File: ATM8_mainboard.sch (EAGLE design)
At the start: 21 parts, among them IC1_POSUV MEGA8-P, IC2_VRETENO MEGA8-P, J1 22-27-2021-02, J2 22-27-2021-02

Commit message: Posledne upravy v dokumente. Nejasne su Dorazy a GVI ci maju byt pripojene na mikrocip alebo priamo len na LPT????
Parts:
- added OUT_POSUV: (no value), con-lstb:MA03-2
- added SV4: (no value), con-lstb:MA05-2
- renumbered SV1 to IO_LPT, SV2 to DISP_1, SV3 to DISP_2
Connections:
- removed net DX: IO_LPT.5
- removed net DZ: IO_LPT.9
- removed net MISO: IC1_POSUV.PB4(MISO), IC2_VRETENO.PB4(MISO), ISP.1, ISP1.1
- removed net MOSI: IC1_POSUV.PB3(MOSI/OC2), IC2_VRETENO.PB3(MOSI/OC2), ISP.4, ISP1.4
- removed net PB0: IC1_POSUV.PB0(ICP), IC2_VRETENO.PB0(ICP)
- removed net PC3: IC1_POSUV.PC3(ADC3), IC2_VRETENO.PC3(ADC3)
- removed net PD0: IC1_POSUV.PD0(RXD)
- removed net PD1: IC1_POSUV.PD1(TXD)
- removed net PD2: IC1_POSUV.PD2(INT0)
- removed net PD3: IC1_POSUV.PD3(INT1), IC2_VRETENO.PD3(INT1)
- removed net PD5: IC1_POSUV.PD5(T1), IC2_VRETENO.PD5(T1)
- removed net PD6: IC1_POSUV.PD6(AIN0), IC2_VRETENO.PD6(AIN0)
- removed net PD7: IC1_POSUV.PD7(AIN1), IC2_VRETENO.PD7(AIN1)
- removed net RESET: IC1_POSUV.PC6(/RESET), IC2_VRETENO.PC6(/RESET), ISP.5, ISP1.5, R1.2, R2.2
- removed net SCK: IC1_POSUV.PB5(SCK), IC2_VRETENO.PB5(SCK), ISP.3, ISP1.3
- removed net SX: IO_LPT.3
- removed net SZ: IO_LPT.7
- new net +Z: IC1_POSUV.PB2(SS/OC1B), OUT_POSUV.5
- new net -Z: IC1_POSUV.PB1(OC1A), OUT_POSUV.3
- new net DIRVRET: IC2_VRETENO.PD6(AIN0)
- new net DIRX: IC1_POSUV.PD0(RXD), IO_LPT.5
- new net DIRZ: IC1_POSUV.PD2(INT0), IO_LPT.9
- new net MISO1: IC1_POSUV.PB4(MISO), ISP.1, OUT_POSUV.6
- new net MISO2: IC2_VRETENO.PB4(MISO), ISP1.1, SV4.9
- new net MOSI1: IC1_POSUV.PB3(MOSI/OC2), ISP.4, OUT_POSUV.4
- new net MOSI2: IC2_VRETENO.PB3(MOSI/OC2), ISP1.4, SV4.7
- new net PB12: IC2_VRETENO.PB1(OC1A)
- new net PB22: IC2_VRETENO.PB2(SS/OC1B)
- new net PC01: IC1_POSUV.PC0(ADC0)
- new net PC02: IC2_VRETENO.PC0(ADC0)
- new net PC11: IC1_POSUV.PC1(ADC1)
- new net PC12: IC2_VRETENO.PC1(ADC1)
- new net PC21: IC1_POSUV.PC2(ADC2)
- new net PC22: IC2_VRETENO.PC2(ADC2)
- new net PC31: IC1_POSUV.PC3(ADC3)
- new net PC32: IC2_VRETENO.PC3(ADC3)
- new net PD32: IC2_VRETENO.PD3(INT1)
- new net PD42: IC2_VRETENO.PD4(XCK/T0)
- new net PD52: IC2_VRETENO.PD5(T1)
- new net PD71: IC1_POSUV.PD7(AIN1)
- new net RESET1: IC1_POSUV.PC6(/RESET), ISP.5, R1.2
- new net RESET2: IC2_VRETENO.PC6(/RESET), ISP1.5, R2.2
- new net SCK1: IC1_POSUV.PB5(SCK), ISP.3
- new net SCK2: IC2_VRETENO.PB5(SCK), ISP1.3, SV4.10
- new net STEPX: IC1_POSUV.PD1(TXD), IO_LPT.3
- new net STEPZ: IC1_POSUV.PD3(INT1), IO_LPT.7
- net DORX: now also IC1_POSUV.PD5(T1)
- net DORZ: now also IC1_POSUV.PD6(AIN0)
- net ENABLE: now also IC1_POSUV.PB0(ICP), IC2_VRETENO.PD7(AIN1)
- net GND: now also OUT_POSUV.1, OUT_POSUV.2, SV4.1, SV4.2
- net PB1: now also SV4.3; no longer IC1_POSUV.PB1(OC1A), IC2_VRETENO.PB1(OC1A)
- net PB2: now also SV4.5; no longer IC1_POSUV.PB2(SS/OC1B), IC2_VRETENO.PB2(SS/OC1B)
- net PC0: now also SV4.8; no longer IC1_POSUV.PC0(ADC0), IC2_VRETENO.PC0(ADC0)
- net PC1: now also SV4.6; no longer IC1_POSUV.PC1(ADC1), IC2_VRETENO.PC1(ADC1)
- net PC2: now also SV4.4; no longer IC1_POSUV.PC2(ADC2), IC2_VRETENO.PC2(ADC2)
- net PD4: no longer IC2_VRETENO.PD4(XCK/T0)
- net PWMV: now also IC2_VRETENO.PB0(ICP)

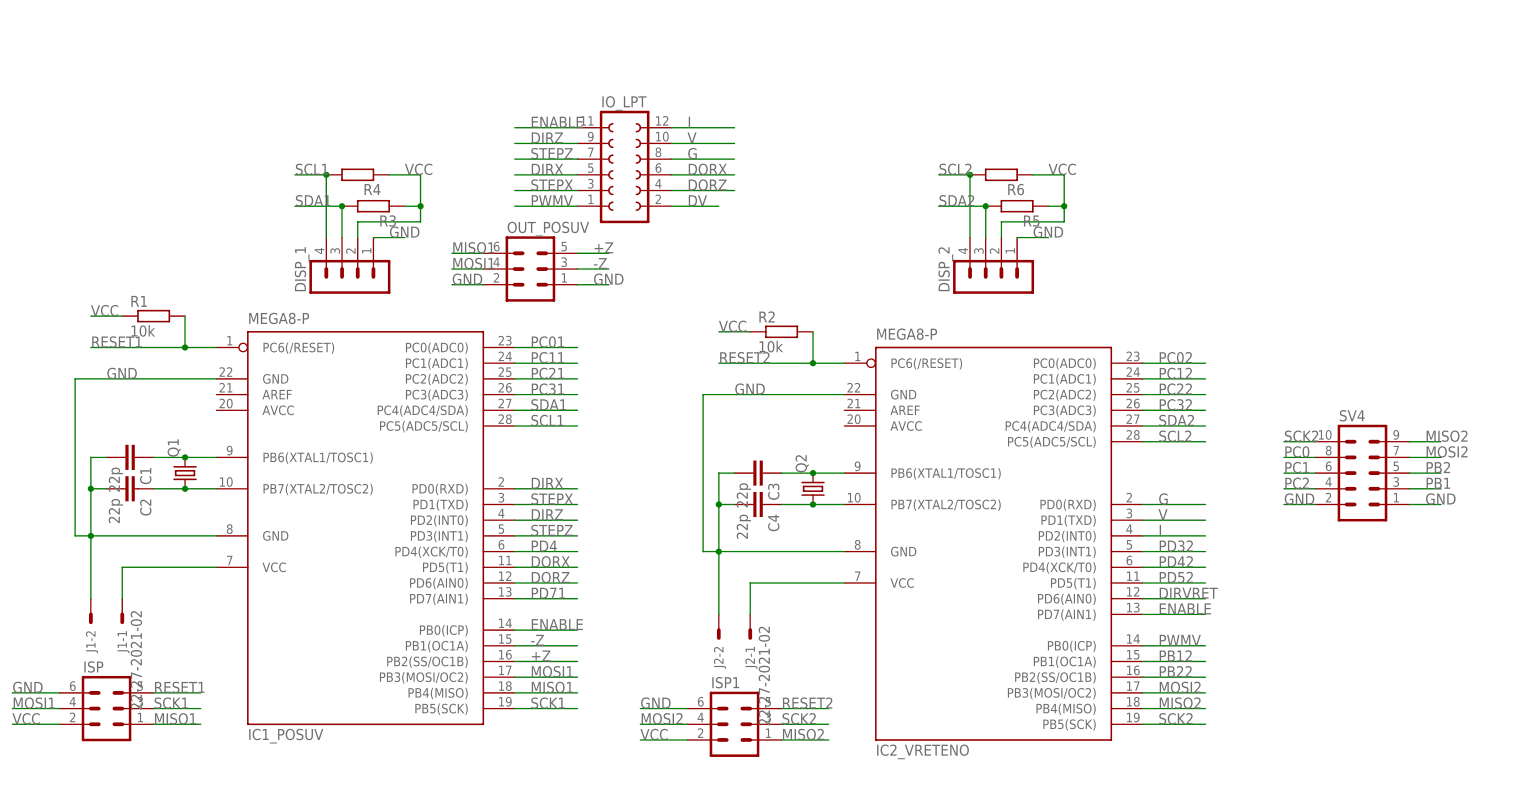
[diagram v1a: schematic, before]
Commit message: Uprava... Pribudlo M01,M02,M03 ale ZMM neviem kam pripojit. Na to sa zabudlo... Predosle problemy pretrvavaju....
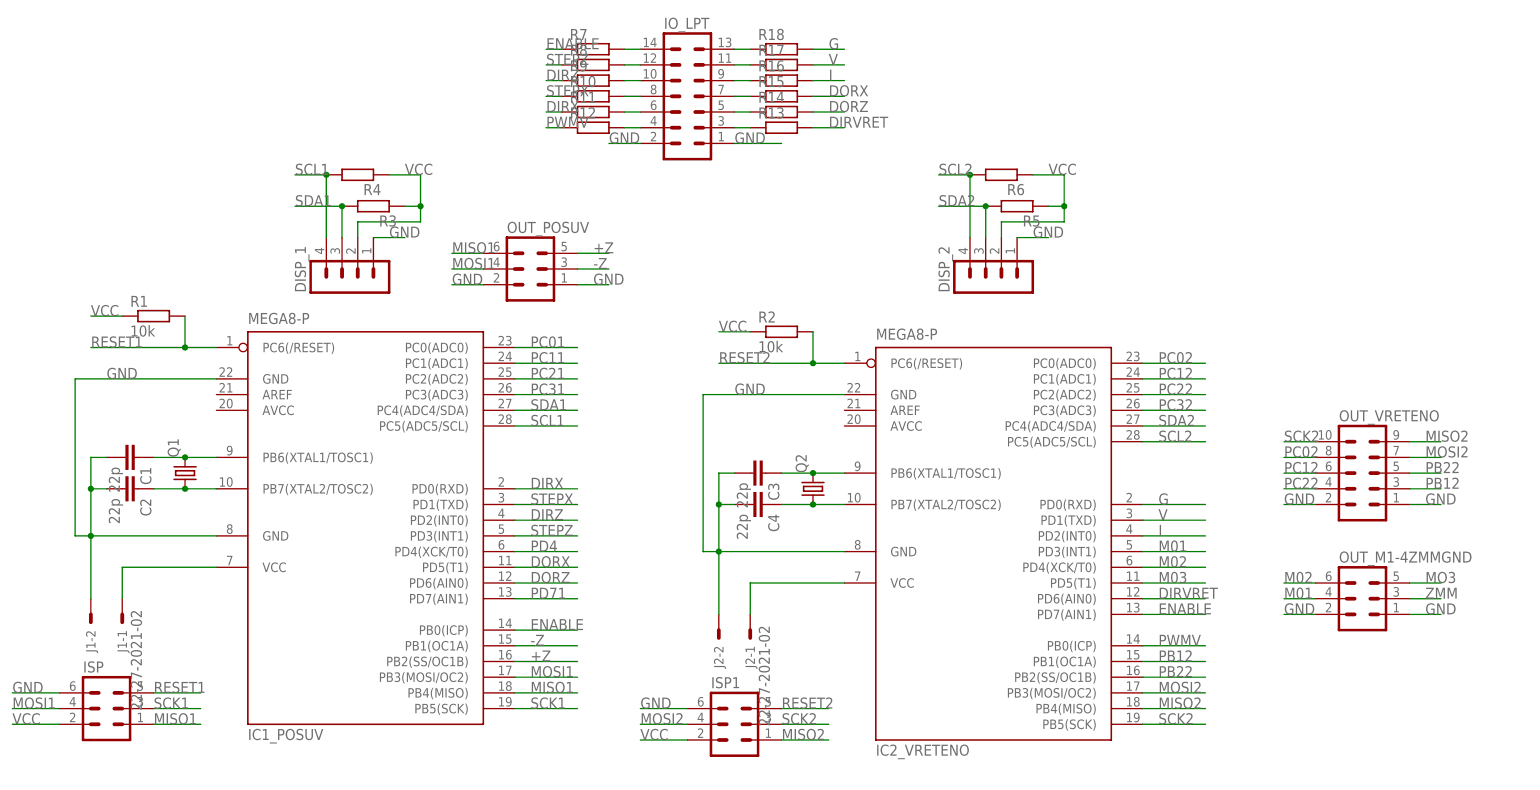
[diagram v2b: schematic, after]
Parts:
- added OUT_M1-4ZMMGND: (no value), con-lstb:MA03-2
- added R10, R11, R12, R13, R14, R15, R16, R17, R18, R7, R8, R9: (no value), resistor:R-EU_0207/10
- IO_LPT: device con-lsta:FE06-2 -> con-lstb:MA07-2
- renumbered SV4 to OUT_VRETENO
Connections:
- net PD52 renamed M03
- removed net DV: IO_LPT.2
- removed net PB1: OUT_VRETENO.3
- removed net PB2: OUT_VRETENO.5
- removed net PC0: OUT_VRETENO.8
- removed net PC1: OUT_VRETENO.6
- removed net PC2: OUT_VRETENO.4
- removed net PD32: IC2_VRETENO.PD3(INT1)
- removed net PD42: IC2_VRETENO.PD4(XCK/T0)
- new net M01: IC2_VRETENO.PD3(INT1), OUT_M1-4ZMMGND.4
- new net M02: IC2_VRETENO.PD4(XCK/T0), OUT_M1-4ZMMGND.6
- new net MO3: OUT_M1-4ZMMGND.5
- new net N$1: IO_LPT.4, R12.2
- new net N$10: IO_LPT.7, R15.1
- new net N$11: IO_LPT.5, R14.1
- new net N$12: IO_LPT.3, R13.1
- new net N$2: IO_LPT.6, R11.2
- new net N$3: IO_LPT.8, R10.2
- new net N$4: IO_LPT.10, R9.2
- new net N$5: IO_LPT.12, R8.2
- new net N$6: IO_LPT.14, R7.2
- new net N$7: IO_LPT.13, R18.1
- new net N$8: IO_LPT.11, R17.1
- new net N$9: IO_LPT.9, R16.1
- new net ZMM: OUT_M1-4ZMMGND.3
- net DIRVRET: now also R13.2
- net DIRX: now also R11.1; no longer IO_LPT.5
- net DIRZ: now also R9.1; no longer IO_LPT.9
- net DORX: now also R15.2; no longer IO_LPT.6
- net DORZ: now also R14.2; no longer IO_LPT.4
- net ENABLE: now also R7.1; no longer IO_LPT.11
- net G: now also R18.2; no longer IO_LPT.8
- net GND: now also IO_LPT.1, IO_LPT.2, OUT_M1-4ZMMGND.1, OUT_M1-4ZMMGND.2
- net I: now also R16.2; no longer IO_LPT.12
- net PB12: now also OUT_VRETENO.3
- net PB22: now also OUT_VRETENO.5
- net PC02: now also OUT_VRETENO.8
- net PC12: now also OUT_VRETENO.6
- net PC22: now also OUT_VRETENO.4
- net PWMV: now also R12.1; no longer IO_LPT.1
- net STEPX: now also R10.1; no longer IO_LPT.3
- net STEPZ: now also R8.1; no longer IO_LPT.7
- net V: now also R17.2; no longer IO_LPT.10

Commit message: 
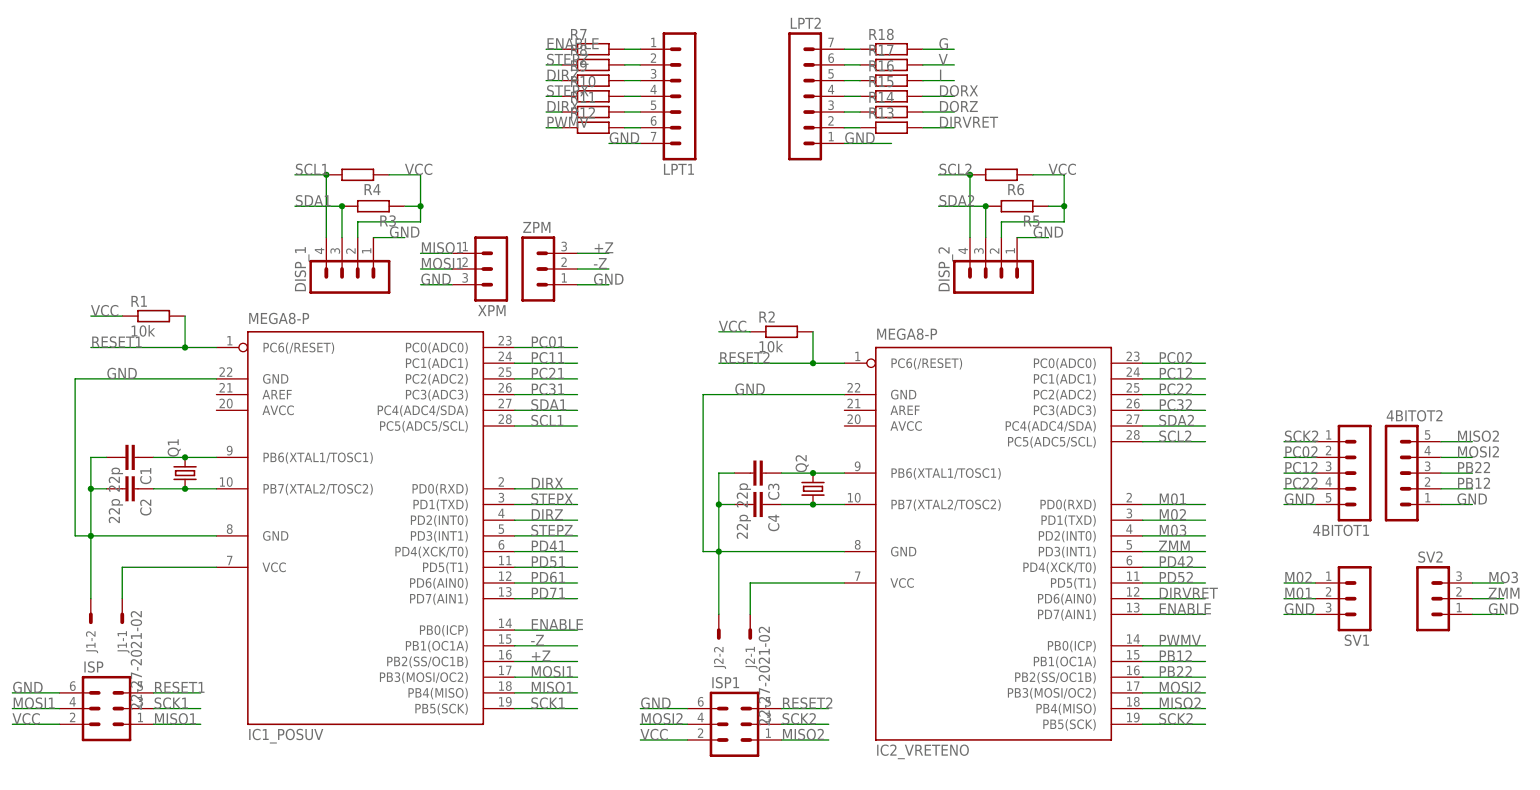
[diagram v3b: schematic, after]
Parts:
- removed IO_LPT: (no value), con-lstb:MA07-2
- removed OUT_M1-4ZMMGND, OUT_POSUV: (no value), con-lstb:MA03-2
- removed OUT_VRETENO: (no value), con-lstb:MA05-2
- added 4BITOT1, 4BITOT2: (no value), con-lstb:MA05-1
- added LPT1, LPT2: (no value), con-lstb:MA07-1
- added SV1, SV2, XPM, ZPM: (no value), con-lstb:MA03-1
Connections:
- net PD4 renamed PD41
- new net PD42: IC2_VRETENO.PD4(XCK/T0)
- new net PD51: IC1_POSUV.PD5(T1)
- new net PD52: IC2_VRETENO.PD5(T1)
- new net PD61: IC1_POSUV.PD6(AIN0)
- net +Z: now also ZPM.3; no longer OUT_POSUV.5
- net -Z: now also ZPM.2; no longer OUT_POSUV.3
- net DORX: no longer IC1_POSUV.PD5(T1)
- net DORZ: no longer IC1_POSUV.PD6(AIN0)
- net G: no longer IC2_VRETENO.PD0(RXD)
- net GND: now also 4BITOT1.5, 4BITOT2.1, LPT1.7, LPT2.1, SV1.3, SV2.1, XPM.3, ZPM.1; no longer IO_LPT.1, IO_LPT.2, OUT_M1-4ZMMGND.1, OUT_M1-4ZMMGND.2, OUT_POSUV.1, OUT_POSUV.2, OUT_VRETENO.1, OUT_VRETENO.2
- net I: no longer IC2_VRETENO.PD2(INT0)
- net M01: now also IC2_VRETENO.PD0(RXD), SV1.2; no longer IC2_VRETENO.PD3(INT1), OUT_M1-4ZMMGND.4
- net M02: now also IC2_VRETENO.PD1(TXD), SV1.1; no longer IC2_VRETENO.PD4(XCK/T0), OUT_M1-4ZMMGND.6
- net M03: now also IC2_VRETENO.PD2(INT0); no longer IC2_VRETENO.PD5(T1)
- net MISO1: now also XPM.1; no longer OUT_POSUV.6
- net MISO2: now also 4BITOT2.5; no longer OUT_VRETENO.9
- net MO3: now also SV2.3; no longer OUT_M1-4ZMMGND.5
- net MOSI1: now also XPM.2; no longer OUT_POSUV.4
- net MOSI2: now also 4BITOT2.4; no longer OUT_VRETENO.7
- net N$1: now also LPT1.6; no longer IO_LPT.4
- net N$10: now also LPT2.4; no longer IO_LPT.7
- net N$11: now also LPT2.3; no longer IO_LPT.5
- net N$12: now also LPT2.2; no longer IO_LPT.3
- net N$2: now also LPT1.5; no longer IO_LPT.6
- net N$3: now also LPT1.4; no longer IO_LPT.8
- net N$4: now also LPT1.3; no longer IO_LPT.10
- net N$5: now also LPT1.2; no longer IO_LPT.12
- net N$6: now also LPT1.1; no longer IO_LPT.14
- net N$7: now also LPT2.7; no longer IO_LPT.13
- net N$8: now also LPT2.6; no longer IO_LPT.11
- net N$9: now also LPT2.5; no longer IO_LPT.9
- net PB12: now also 4BITOT2.2; no longer OUT_VRETENO.3
- net PB22: now also 4BITOT2.3; no longer OUT_VRETENO.5
- net PC02: now also 4BITOT1.2; no longer OUT_VRETENO.8
- net PC12: now also 4BITOT1.3; no longer OUT_VRETENO.6
- net PC22: now also 4BITOT1.4; no longer OUT_VRETENO.4
- net SCK2: now also 4BITOT1.1; no longer OUT_VRETENO.10
- net V: no longer IC2_VRETENO.PD1(TXD)
- net ZMM: now also IC2_VRETENO.PD3(INT1), SV2.2; no longer OUT_M1-4ZMMGND.3
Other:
- moved on the sheet: R13, R14, R15, R16, R17, R18

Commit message: 
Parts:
- added FREE1, INPUTCNC: FEMALE, con-lstb:MA05-1
- added FREE2: MALE, jumper:JP1E
- added SV4: FEMALE, con-lstb:MA04-1
- 4BITOT1, 4BITOT2, LPT1, LPT2, SV1, SV2, XPM, ZPM: value (none) -> FEMALE
- DISP_1, DISP_2, ISP, ISP1: value (none) -> MALE
- R11, R12, R13, R14, R15, R16, R17, R18, R7, R8, R9: value (none) -> 270R
- R3, R4, R5, R6: value (none) -> 4.7k
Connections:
- net DORX: now also INPUTCNC.4
- net DORZ: now also INPUTCNC.5
- net G: now also INPUTCNC.1
- net I: now also INPUTCNC.3
- net PC01: now also FREE1.1
- net PC11: now also FREE1.2
- net PC21: now also FREE1.3
- net PC31: now also FREE1.4
- net PD41: now also SV4.1
- net PD42: now also FREE2.1
- net PD51: now also SV4.2
- net PD52: now also FREE2.2
- net PD61: now also SV4.3
- net PD71: now also SV4.4
- net SCK1: now also FREE1.5
- net V: now also INPUTCNC.2
